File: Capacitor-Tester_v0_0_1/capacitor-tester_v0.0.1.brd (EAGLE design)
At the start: 67 x 45 mm, 34 parts, among them IC1 AD8531ARZ, IC2 MC34063EBD-TR, IC3 DAC6571IDBVT, IC5 AD8397ARDZ, J1 USB4125-GF-A-0190_REVA2, J2 DS1044-140G, J4 250-103, U1 AD5933, Y1 LFSPXO018034

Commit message: v0.0.1 - CMD renumber + tnames + bnames
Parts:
- removed IC5: AD8397ARDZ, AD8397ARDZ:SOIC127P600X175-9N
- removed J4: 250-103, custom_library:CONN3_250-103_WAG
- removed R15, R16: 10k-1%, custom_library:R0603
- added IC4: MC34063EBD-TR, MC34063EBD-TR:SOIC127P600X175-8N
- added J3: USB4125-GF-A-0190_REVA2, USB-C-6Pin:GCT_USB4125-GF-A-0190_REVA2
- added R7, R8: DNP-4k7-1%, custom_library:R0603
- C2: value 10u -> 100n
- C3: value 100n -> 10u
- C4: value 270u / 16V -> 10u; device EEEFKC271XSP:EEE0JA331XP -> custom_library:C0603
- C5: value 270u / 16V -> 100n; device EEEFKC271XSP:EEE0JA331XP -> custom_library:C0603
- C6: value 560p -> 270u / 16V; device custom_library:C0603 -> EEEFKC271XSP:EEE0JA331XP
- C7: value 100n -> 560p
- C8: value 10u -> 270u / 16V; device custom_library:C0603 -> EEEFKC271XSP:EEE0JA331XP
- D1: value SS14 -> PMEG6020ER,115; device SS14:DIOM5227X270N -> PMEG6020ER_115:PMEG6020ER115
- D2: value PMEG6020ER,115 -> SS14; device PMEG6020ER_115:PMEG6020ER115 -> SS14:DIOM5227X270N
- IC1: value AD8531ARZ -> DAC6571IDBVT; device AD8531ARZ:SOIC127P600X175-8N -> DAC6571IDBVT:SOT95P280X145-6N
- IC2: value MC34063EBD-TR -> AD8397ARDZ; device MC34063EBD-TR:SOIC127P600X175-8N -> AD8397ARDZ:SOIC127P600X175-9N
- IC3: value DAC6571IDBVT -> AD8531ARZ; device DAC6571IDBVT:SOT95P280X145-6N -> AD8531ARZ:SOIC127P600X175-8N
- J1: value USB4125-GF-A-0190_REVA2 -> DS1044-140G; device USB-C-6Pin:GCT_USB4125-GF-A-0190_REVA2 -> DS1044-140G:CONNFLY_DS1044-140G
- J2: value DS1044-140G -> 250-103; device DS1044-140G:CONNFLY_DS1044-140G -> custom_library:CONN3_250-103_WAG
- R1, R3: value DNP-4k7-1% -> 10k-1%
- R10: value 1k-1% -> R133-1%
- R11: value R133-1% -> 8k66-1%
- R12: value 180R-1% -> 1k-1%
- R2: value 10k-1% -> DNP-10k-1%
- R4: value DNP-10k-1% -> 1k-1%
- R6: value 1k-1% -> 10k-1%
- R9: value 8k66-1% -> 180R-1%
- moved R4 49.3 mm to (56.8, 22.1), turned to 90 degrees
- moved R1 48.7 mm to (59.6, 35.5), turned to 90 degrees
- moved IC1 40.3 mm to (46.6, 38.1)
- moved IC3 40.3 mm to (8.00, 26.6)
- moved J1 40.1 mm to (45.5, 7.99), turned to 90 degrees
- moved C2 36.3 mm to (7.05, 33.1), turned to 90 degrees
- moved IC2 35.4 mm to (59.0, 28.8), flipped to the top, turned to 90 degrees
- moved C4 30.4 mm to (42.1, 24.0), flipped to the top, turned to 0 degrees
- moved J2 29.8 mm to (15.8, 5.40), turned to 0 degrees
- moved R3 20.8 mm to (10.8, 32.9), turned to 90 degrees
- moved C1 19.9 mm to (57.0, 35.5), turned to 90 degrees
- moved C5 17.6 mm to (42.1, 22.4), flipped to the top, turned to 0 degrees
- moved C8 13.3 mm to (36.0, 38.8), flipped to the bottom, turned to 90 degrees
- moved D1 13.3 mm to (7.25, 19.5), flipped to the top
- moved D2 13.3 mm to (18.7, 26.2), flipped to the bottom
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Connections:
- net +12V: now also C1.1, C6.1, D2.1, IC2.8, R11.1; no longer C3.1, C4.1, D1.1, IC5.8, R9.1
- net +5V: now also C3.1, C4.1, D1.1, IC1.3, IC3.7, IC4.6, J3.A9, J3.B9, R10.1, R7.2, R8.2; no longer C1.1, C7.1, D2.1, IC1.7, IC2.6, IC3.3, J1.A9, J1.B9, R1.2, R11.1, R3.2
- net DAC_OUT: now also IC1.1, IC2.5; no longer IC3.1, IC5.5
- net FUNC_GEN: now also J2.3, SJ1.1; no longer J4.3, SJ2.1
- net GND: now also IC1.2, IC1.6, IC2.9, IC3.3, IC3.4, IC4.2, IC4.4, J3.A12, J3.B12, J3.S1, J3.S2, J3.S3, J3.S4, R1.2, R12.2; no longer IC1.3, IC1.4, IC2.2, IC3.2, IC3.6, IC5.4, IC5.9, J1.A12, J1.B12, J1.S1, J1.S2, J1.S3, J1.S4, R10.2, R15.2
- net MCLK: now also SJ2.1; no longer SJ1.1
- net N$1: now also IC3.6, R2.2, R3.1; no longer IC1.6, R2.1, R4.2
- net N$10: now also C7.1, IC4.3; no longer C6.1, IC2.3
- net N$11: now also IC4.7, R10.2, R9.2; no longer IC2.7, R11.2, R12.2
- net N$13: now also IC2.6, R1.1, R6.2; no longer IC5.6, R15.1, R16.2
- net N$4: now also IC2.2, R4.1; no longer IC5.2, R6.1
- net N$5: now also D2.2, IC4.1; no longer D1.2, IC2.1
- net N$7: now also IC4.5, R11.2, R12.1; no longer IC2.5, R10.1, R9.2
- net N$8: now also IC4.8, R9.1; no longer IC2.8, R12.1
- net SCL: now also IC1.5, J2.2, R8.1; no longer IC3.5, J4.2, R1.1
- net SDA: now also IC1.4, J2.1, R7.1; no longer IC3.4, J4.1, R3.1
- net UZA_OUT: now also IC2.1, J1.1, J1.2, J1.3, J1.4, J1.5, J1.6, J1.7, R4.2; no longer IC5.1, J2.1, J2.2, J2.3, J2.4, J2.5, J2.6, J2.7, R6.2
- net UZB_OUT: now also IC2.3, IC2.7, R6.1; no longer IC5.3, IC5.7, R16.1
- net VIN: now also R2.1; no longer R4.1
- net Z_OUT: now also D1.2, IC3.2, J1.10, J1.11, J1.12, J1.13, J1.14, J1.8, J1.9, R3.2; no longer D2.2, IC1.2, J2.10, J2.11, J2.12, J2.13, J2.14, J2.8, J2.9, R2.2

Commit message: v0.0.1 - Added text to the Solder Jumpers
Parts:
- moved SJ2 0.20 mm to (24.1, 21.0)
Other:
- board text added: "FUNC GEN"
- board text added: "MCLK"
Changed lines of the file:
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@@
 <layer number="14" name="Route14" color="1" fill="6" visible="no" active="no"/>
 <layer number="15" name="Route15" color="4" fill="6" visible="no" active="no"/>
-<layer number="16" name="Bottom" color="1" fill="1" visible="yes" active="yes"/>
+<layer number="16" name="Bottom" color="1" fill="1" visible="no" active="yes"/>
 <layer number="17" name="Pads" color="2" fill="1" visible="yes" active="yes"/>
 <layer number="18" name="Vias" color="2" fill="1" visible="yes" active="yes"/>
@@
 <layer number="20" name="Dimension" color="24" fill="1" visible="yes" active="yes"/>
 <layer number="21" name="tPlace" color="7" fill="1" visible="yes" active="yes"/>
-<layer number="22" name="bPlace" color="7" fill="1" visible="yes" active="yes"/>
+<layer number="22" name="bPlace" color="7" fill="1" visible="no" active="yes"/>
 <layer number="23" name="tOrigins" color="15" fill="1" visible="yes" active="yes"/>
-<layer number="24" name="bOrigins" color="15" fill="1" visible="yes" active="yes"/>
+<layer number="24" name="bOrigins" color="15" fill="1" visible="no" active="yes"/>
 <layer number="25" name="tNames" color="7" fill="1" visible="yes" active="yes"/>
-<layer number="26" name="bNames" color="7" fill="1" visible="yes" active="yes"/>
+<layer number="26" name="bNames" color="7" fill="1" visible="no" active="yes"/>
 <layer number="27" name="tValues" color="7" fill="1" visible="no" active="yes"/>
 <layer number="28" name="bValues" color="7" fill="1" visible="no" active="yes"/>
@@
 <layer number="38" name="bTest" color="7" fill="1" visible="no" active="yes"/>
 <layer number="39" name="tKeepout" color="4" fill="11" visible="yes" active="yes"/>
-<layer number="40" name="bKeepout" color="1" fill="11" visible="yes" active="yes"/>
+<layer number="40" name="bKeepout" color="1" fill="11" visible="no" active="yes"/>
 <layer number="41" name="tRestrict" color="4" fill="10" visible="yes" active="yes"/>
-<layer number="42" name="bRestrict" color="1" fill="10" visible="yes" active="yes"/>
+<layer number="42" name="bRestrict" color="1" fill="10" visible="no" active="yes"/>
 <layer number="43" name="vRestrict" color="2" fill="10" visible="no" active="yes"/>
 <layer number="44" name="Drills" color="7" fill="1" visible="no" active="yes"/>
@@
 <layer number="49" name="Reference" color="7" fill="1" visible="no" active="yes"/>
 <layer number="51" name="tDocu" color="7" fill="1" visible="yes" active="yes"/>
-<layer number="52" name="bDocu" color="7" fill="1" visible="yes" active="yes"/>
+<layer number="52" name="bDocu" color="7" fill="1" visible="no" active="yes"/>
 <layer number="88" name="SimResults" color="9" fill="1" visible="no" active="no"/>
 <layer number="89" name="SimProbes" color="9" fill="1" visible="no" active="no"/>
@@
 <wire x1="67" y1="45" x2="0" y2="45" width="0" layer="20"/>
 <wire x1="0" y1="45" x2="0" y2="0" width="0" layer="20"/>
+<text x="17.4" y="23.4" size="1.27" layer="21" font="vector" ratio="16">FUNC
+GEN</text>
+<text x="17.2" y="20.6" size="1.27" layer="21" font="vector" ratio="16">MCLK</text>
+<wire x1="26.6" y1="23" x2="17.2" y2="23" width="0.4064" layer="21"/>
 </plain>
 <attributes>
@@
 <attribute name="VALUE" x="33.991" y="34.254" size="1.27" layer="27" align="center"/>
 </element>
-<element name="SJ2" library="jumper" library_urn="urn:adsk.eagle:library:252" package="SJW" package3d_urn="urn:adsk.eagle:package:15507/1" value="" x="24.131" y="21.154" smashed="yes">
-<attribute name="NAME" x="21.268" y="20.372" size="0.8" layer="25" ratio="10" rot="R90"/>
-<attribute name="POPULARITY" value="3" x="24.131" y="21.154" size="1.778" layer="27" display="off"/>
-<attribute name="VALUE" x="25.131" y="21.154" size="0.02" layer="27"/>
+<element name="SJ2" library="jumper" library_urn="urn:adsk.eagle:library:252" package="SJW" package3d_urn="urn:adsk.eagle:package:15507/1" value="" x="24.131" y="20.954" smashed="yes">
+<attribute name="NAME" x="25.028" y="19.068" size="0.8" layer="25" ratio="10" rot="R180"/>
+<attribute name="POPULARITY" value="3" x="24.131" y="20.954" size="1.778" layer="27" display="off"/>
+<attribute name="VALUE" x="25.131" y="20.954" size="0.02" layer="27"/>
 </element>
 <element name="SJ1" library="jumper" library_urn="urn:adsk.eagle:library:252" package="SJW" package3d_urn="urn:adsk.eagle:package:15507/1" value="" x="24.131" y="24.954" smashed="yes">
-<attribute name="NAME" x="21.468" y="24.372" size="0.8" layer="25" ratio="10" rot="R90"/>
+<attribute name="NAME" x="25.228" y="27.668" size="0.8" layer="25" ratio="10" rot="R180"/>
 <attribute name="POPULARITY" value="3" x="24.131" y="24.954" size="1.778" layer="27" display="off"/>
 <attribute name="VALUE" x="25.131" y="24.954" size="0.02" layer="27"/>
@@
 <wire x1="21.5436" y1="12.1528" x2="21.5436" y2="4.6954" width="0.4" layer="1"/>
 <wire x1="22.6484" y1="13.2576" x2="21.5436" y2="12.1528" width="0.4" layer="1"/>
-<wire x1="22.6484" y1="20.9912" x2="22.6484" y2="13.2576" width="0.4" layer="1"/>
+<wire x1="22.6484" y1="20.7912" x2="22.6484" y2="13.2576" width="0.4" layer="1"/>
 <wire x1="36.4584" y1="36.1822" x2="36.531" y2="36.354" width="0.4" layer="1"/>
-<wire x1="22.6484" y1="20.9912" x2="22.861" y2="21.154" width="0.4" layer="1"/>
+<wire x1="22.6484" y1="20.7912" x2="22.861" y2="20.954" width="0.4" layer="1"/>
 </signal>
 <signal name="FUNC_GEN">
@@
 <contactref element="U1" pad="8"/>
 <wire x1="27.0676" y1="22.9246" x2="30.382" y2="22.9246" width="0.4" layer="1"/>
-<wire x1="25.4104" y1="21.2674" x2="26.9295" y2="22.7865" width="0.4" layer="1"/>
+<wire x1="25.428478125" y1="21.285478125" x2="26.9295" y2="22.7865" width="0.4" layer="1"/>
 <wire x1="26.9295" y1="22.7865" x2="27.0676" y2="22.9246" width="0.4" layer="1"/>
 <wire x1="30.382" y1="22.9246" x2="30.521" y2="22.904" width="0.4" layer="1"/>
-<wire x1="25.4104" y1="21.2674" x2="25.401" y2="21.154" width="0.4" layer="1"/>
+<wire x1="25.428478125" y1="21.285478125" x2="25.401" y2="20.954" width="0.4" layer="1"/>
 <wire x1="25.4104" y1="24.3056" x2="25.4104" y2="24.858" width="0.4" layer="1"/>
 <wire x1="26.9295" y1="22.7865" x2="25.4104" y2="24.3056" width="0.4" layer="1"/>
@@
 </drawing>
 <compatibility>
+<note version="6.3" minversion="6.2.2" severity="warning">
+Since Version 6.2.2 text objects can contain more than one line,
+which will not be processed correctly with this version.
+</note>
 <note version="8.2" severity="warning">
 Since Version 8.2, EAGLE supports online libraries. The ids

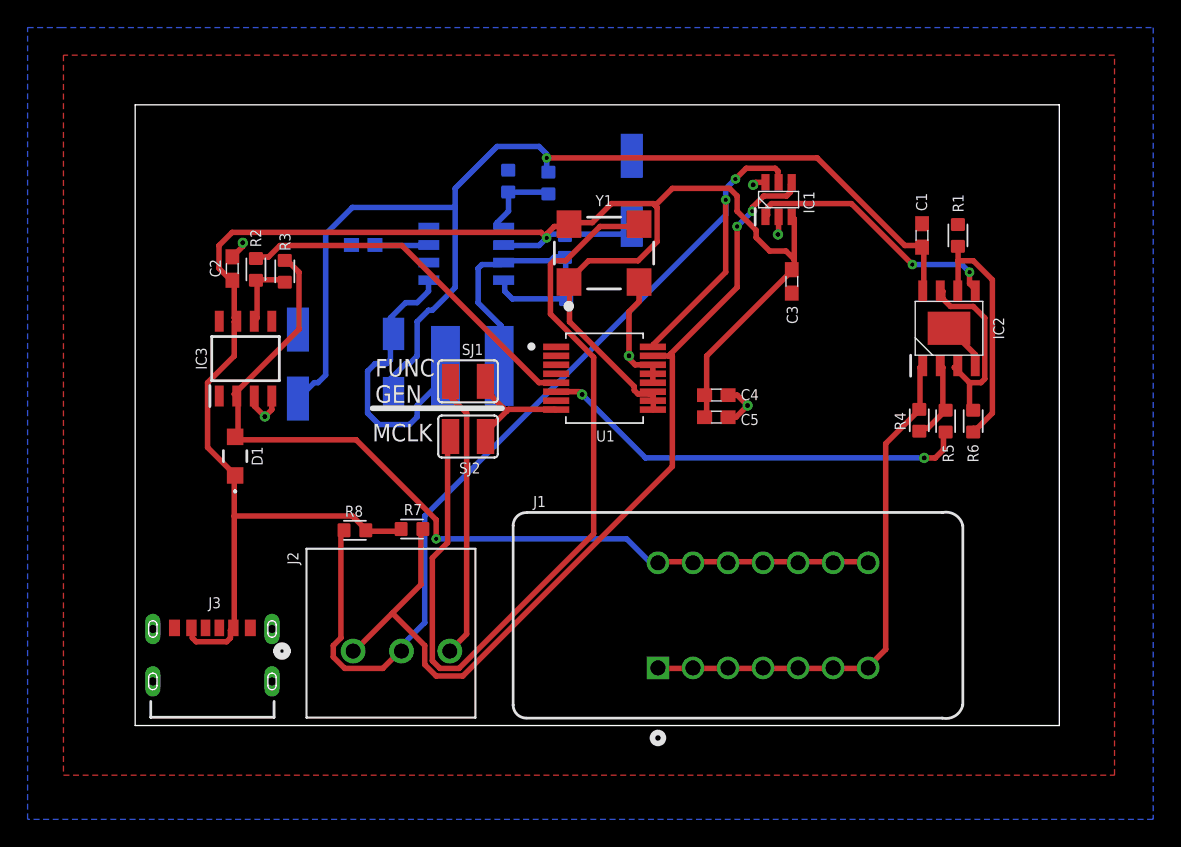
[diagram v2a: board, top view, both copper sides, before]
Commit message: v0.0.1 - Trying different component layout. Finished brd
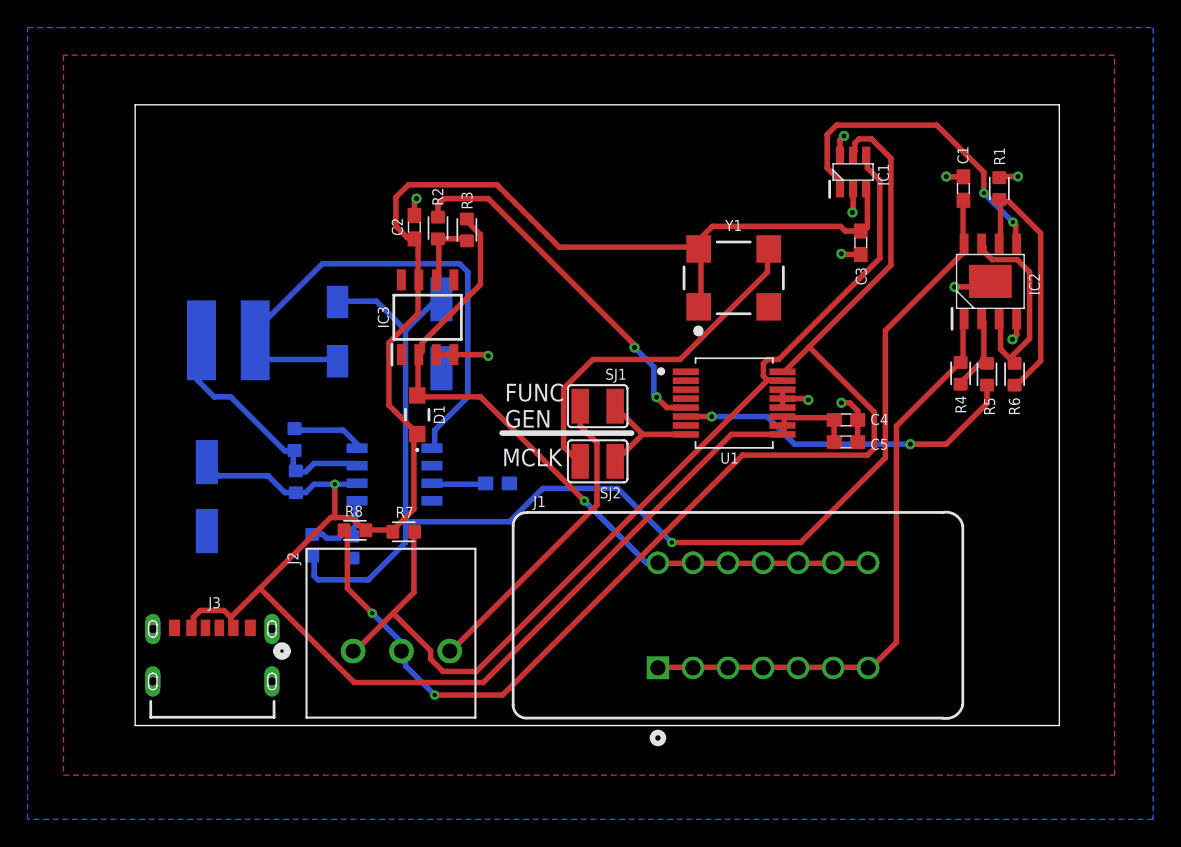
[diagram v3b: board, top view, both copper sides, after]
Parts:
- moved C8 38.0 mm to (5.20, 16.6), turned to 270 degrees
- moved R11 31.3 mm to (12.8, 13.1), turned to 90 degrees
- moved R12 28.8 mm to (15.8, 12.9), turned to 270 degrees
- moved R10 25.9 mm to (11.6, 17.7), turned to 90 degrees
- moved R9 22.5 mm to (11.6, 20.7), turned to 270 degrees
- moved C7 19.8 mm to (26.3, 17.6), turned to 180 degrees
- moved L1 17.8 mm to (6.75, 27.9), turned to 90 degrees
- moved IC4 16.8 mm to (18.8, 18.2), turned to 0 degrees
- moved D1 13.5 mm to (20.4, 22.5)
- moved R2 13.5 mm to (22.0, 36.1)
- moved C2 13.5 mm to (20.2, 36.1)
- moved IC3 13.5 mm to (21.2, 29.6)
- moved R3 13.5 mm to (24.0, 35.9)
- moved C6 10.6 mm to (22.2, 28.4), turned to 270 degrees
- moved C4 9.57 mm to (51.5, 22.2)
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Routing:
- net MCLK: track 61.3 -> 25.8 mm
- net N$5: track 21.4 -> 39.3 mm
- net +5V: track 144.9 -> 162.4 mm
- net Z_OUT: track 66.3 -> 52.9 mm
- net +12V: track 82.9 -> 95.2 mm
- net SCL: track 76.8 -> 86.2 mm
- net VOUT: track 31.7 -> 25.2 mm
- net UZA_OUT: track 38.9 -> 43.6 mm
- net DAC_OUT: track 19.1 -> 23.7 mm
- net SDA: track 66.9 -> 70.5 mm, vias 2 -> 0
- net N$11: track 15.9 -> 18.5 mm
- net FUNC_GEN: track 20.5 -> 22.7 mm
- net UZB_OUT: track 14.0 -> 15.4 mm
- net N$13: track 18.1 -> 19.0 mm
- net GND: track 23.2 -> 23.6 mm, vias 6 -> 11
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
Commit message: v0.0.1 - Different component layout and trace placement
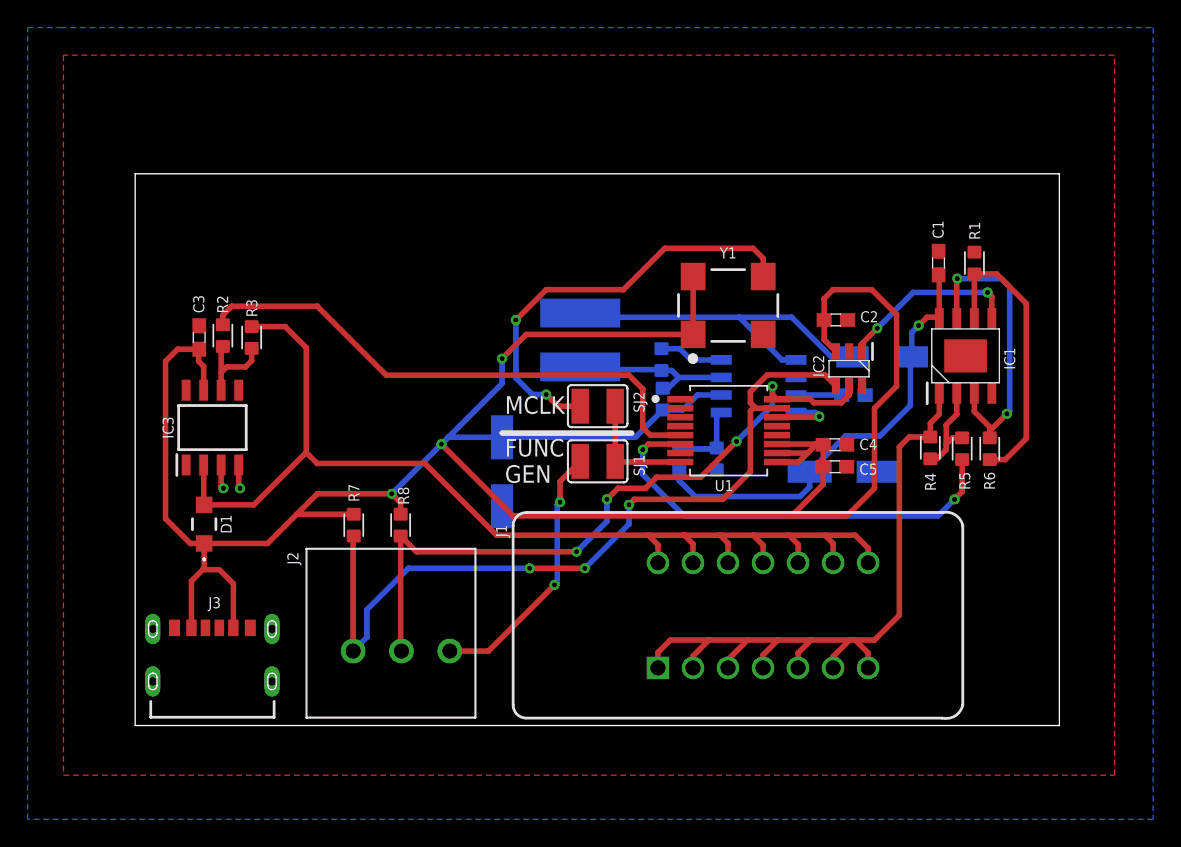
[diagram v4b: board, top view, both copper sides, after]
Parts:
- C2: value 100n -> 10u
- C3: value 10u -> 100n
- C7: value 560p -> 270u / 16V; device custom_library:C0603 -> EEEFKC271XSP:EEE0JA331XP
- C8: value 270u / 16V -> 560p; device EEEFKC271XSP:EEE0JA331XP -> custom_library:C0603
- IC1: value DAC6571IDBVT -> AD8397ARDZ; device DAC6571IDBVT:SOT95P280X145-6N -> AD8397ARDZ:SOIC127P600X175-9N
- IC2: value AD8397ARDZ -> DAC6571IDBVT; device AD8397ARDZ:SOIC127P600X175-9N -> DAC6571IDBVT:SOT95P280X145-6N
- R10: value R133-1% -> 1k-1%
- R11: value 8k66-1% -> R133-1%
- R12: value 1k-1% -> 180R-1%
- R9: value 180R-1% -> 8k66-1%
- moved C3 48.4 mm to (4.65, 28.1), turned to 90 degrees
- moved C8 47.4 mm to (52.1, 24.0), turned to 180 degrees
- moved D2 39.5 mm to (54.2, 26.7), turned to 0 degrees
- moved C2 31.3 mm to (50.8, 29.4), turned to 0 degrees
- moved C6 30.9 mm to (51.4, 18.4), turned to 180 degrees
- moved R10 30.6 mm to (42.2, 19.3), turned to 270 degrees
- moved R9 27.9 mm to (39.4, 19.3), turned to 90 degrees
- moved R11 27.5 mm to (38.2, 23.7)
- moved IC4 27.2 mm to (45.2, 24.6)
- moved R12 26.2 mm to (38.2, 26.5)
- moved L1 25.5 mm to (32.3, 28.0), turned to 0 degrees
- moved IC3 17.5 mm to (5.60, 21.6)
- moved R2 17.4 mm to (6.35, 28.3)
- moved R3 17.4 mm to (8.45, 28.1)
- moved D1 17.4 mm to (5.00, 14.6)
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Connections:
- net +12V: now also IC1.8, R9.1; no longer IC2.8, R11.1
- net +5V: now also C7.1, IC2.3, R11.1; no longer C8.1, IC1.3, R10.1
- net DAC_OUT: now also IC1.5, IC2.1; no longer IC1.1, IC2.5
- net FUNC_GEN: now also SJ2.1; no longer SJ1.1
- net GND: now also IC1.4, IC1.9, IC2.2, IC2.6, R10.2; no longer IC1.2, IC1.6, IC2.4, IC2.9, R12.2
- net MCLK: now also SJ1.1; no longer SJ2.1
- net N$10: now also C8.1; no longer C7.1
- net N$11: now also R11.2, R12.2; no longer R10.2, R9.2
- net N$13: now also IC1.6; no longer IC2.6
- net N$4: now also IC1.2; no longer IC2.2
- net N$7: now also R10.1, R9.2; no longer R11.2, R12.1
- net N$8: now also R12.1; no longer R9.1
- net SCL: now also IC2.5; no longer IC1.5
- net SDA: now also IC2.4; no longer IC1.4
- net UZA_OUT: now also IC1.1; no longer IC2.1
- net UZB_OUT: now also IC1.3, IC1.7; no longer IC2.3, IC2.7
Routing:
- net +12V: track 95.2 -> 32.3 mm
- net SCL: track 86.2 -> 49.8 mm, vias 2 -> 4
- net Z_OUT: track 52.9 -> 82.4 mm, vias 1 -> 0
- net +5V: track 162.4 -> 180.2 mm, vias 1 -> 3
- net GND: track 23.6 -> 8.38 mm, vias 11 -> 3
- net VIN: track 26.6 -> 39.6 mm, vias 2 -> 0
- net N$5: track 39.3 -> 26.4 mm
- net SDA: track 70.5 -> 59.3 mm, vias 0 -> 3
- net DAC_OUT: track 23.7 -> 13.2 mm
- net UZA_OUT: track 43.6 -> 52.8 mm
- net VOUT: track 25.2 -> 32.1 mm
- net UZB_OUT: track 15.4 -> 22.2 mm, vias 0 -> 2
- net N$11: track 18.5 -> 12.0 mm
- net MCLK: track 25.8 -> 31.4 mm, vias 0 -> 2
- net FUNC_GEN: track 22.7 -> 19.3 mm, vias 0 -> 2
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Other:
- board size 67 x 45 mm -> 67 x 40 mm
